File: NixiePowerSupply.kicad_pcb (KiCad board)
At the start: 2 copper layers, 50.8 x 44.4 mm, 20 parts, among them J1 BARREL_JACK, P1 CONN_01X03, P2 CONN_01X02, T1 IRF644, U1 MAX1771

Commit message: Routing complete
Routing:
- net GND: track 38.7 -> 39.5 mm
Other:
- board text added: "+12V SHDN GND"
- board text added: "HV- HV+"
- board text added: "NixMaster 9000 Rev 1.0 Carl Raymond, May 2017"
- board text added: "OUT ADJ. 150-200V"
- board text added: "PWR 12V"
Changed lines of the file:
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@@
-(kicad_pcb (version 4) (host pcbnew 4.0.6)
+(kicad_pcb (version 4) (host pcbnew 4.0.5)
   (general
     (links 32)
-    (no_connects 3)
+    (no_connects 0)
     (area 40.384999 24.805 99.568572 72.195)
     (thickness 1.6)
-    (drawings 4)
+    (drawings 9)
     (tracks 94)
     (zones 0)
@@
   )
   (setup
-    (last_trace_width 1.016)
+    (last_trace_width 0.508)
     (user_trace_width 0.508)
     (user_trace_width 1.016)
@@
     (trace_clearance 0.2)
     (zone_clearance 0.254)
-    (zone_45_only no)
+    (zone_45_only yes)
     (trace_min 0.2)
     (segment_width 0.2)
@@
     (mod_text_size 1 1)
     (mod_text_width 0.15)
-    (pad_size 1.5 1.5)
-    (pad_drill 0.6)
+    (pad_size 3.7 3.7)
+    (pad_drill 3.7)
     (pad_to_mask_clearance 0)
     (aux_axis_origin 0 0)
     (visible_elements 7FFFFFFF)
     (pcbplotparams
-      (layerselection 0x00030_80000001)
-      (usegerberextensions false)
+      (layerselection 0x010f0_80000001)
+      (usegerberextensions true)
       (excludeedgelayer true)
       (linewidth 0.100000)
@@
       (plotinvisibletext false)
       (padsonsilk false)
-      (subtractmaskfromsilk false)
+      (subtractmaskfromsilk true)
       (outputformat 1)
       (mirror false)
-      (drillshape 1)
+      (drillshape 0)
       (scaleselection 1)
       (outputdirectory ""))
@@
     (tags "resistor 0805")
     (attr smd)
-    (fp_text reference R1 (at 3.175 0 360) (layer F.SilkS)
+    (fp_text reference R1 (at -3.302 0 360) (layer F.SilkS)
       (effects (font (size 1 1) (thickness 0.15)))
     )
@@
   (module nixie:Trimpot_Bourns_3214W (layer F.Cu)
     (at 72.771 57.912)
-    (fp_text reference VR1 (at 0.127 3.937) (layer F.SilkS)
+    (fp_text reference VR1 (at 0.10668 -2.9972) (layer F.SilkS)
       (effects (font (size 1 1) (thickness 0.15)))
     )
@@
   (module nixie:L-B82479A1 (layer F.Cu)
     (at 58.928 38.1 45)
-    (fp_text reference L1 (at 7.112 7.112 225) (layer F.SilkS)
+    (fp_text reference L1 (at -6.64539 -6.64539 315) (layer F.SilkS)
       (effects (font (size 1 1) (thickness 0.15)))
     )
@@
     (tags "SOIC 1.27")
     (attr smd)
-    (fp_text reference U1 (at 0 -3.5) (layer F.SilkS)
+    (fp_text reference U1 (at 0 3.937) (layer F.SilkS)
       (effects (font (size 1 1) (thickness 0.15)))
     )
@@
     (tags "capacitor 0805")
     (attr smd)
-    (fp_text reference C2 (at 3.302 -0.127 360) (layer F.SilkS)
+    (fp_text reference C2 (at 4.29768 0.04572 360) (layer F.SilkS)
       (effects (font (size 1 1) (thickness 0.15)))
     )
@@
     (fp_circle (center 0 0) (end 3.7 0) (layer Cmts.User) (width 0.15))
     (fp_circle (center 0 0) (end 3.95 0) (layer F.CrtYd) (width 0.05))
-    (pad 1 np_thru_hole circle (at 0 0) (size 3.7 3.7) (drill 3.7) (layers *.Cu *.Mask))
+    (pad "" np_thru_hole circle (at 0 0) (size 3.7 3.7) (drill 3.7) (layers *.Cu *.Mask))
   )
   (module Resistors_SMD:R_2010_HandSoldering (layer F.Cu)
@@
     (tags "resistor 2010")
     (attr smd)
-    (fp_text reference Rsense1 (at 5.461 -0.254 360) (layer F.SilkS)
+    (fp_text reference Rsense1 (at -1.143 -1.905 450) (layer F.SilkS)
       (effects (font (size 1 1) (thickness 0.15)))
     )
@@
     (descr "SMT capacitor, aluminium electrolytic, 10x10")
     (attr smd)
-    (fp_text reference C4 (at 0 6.46) (layer F.SilkS)
+    (fp_text reference C4 (at -1.524 -6.096) (layer F.SilkS)
       (effects (font (size 1 1) (thickness 0.15)))
     )
@@
     )
   )
+  (gr_text "OUT ADJ.\n150-200V" (at 72.87768 61.63056) (layer F.SilkS)
+    (effects (font (size 0.762 0.762) (thickness 0.1778)))
+  )
+  (gr_text "PWR\n12V" (at 47.625 45.72) (layer F.SilkS)
+    (effects (font (size 1.5 1.5) (thickness 0.3)))
+  )
+  (gr_text "HV-\n\n\n\nHV+" (at 80.01 62.23 90) (layer F.SilkS)
+    (effects (font (size 0.762 1) (thickness 0.1778)))
+  )
+  (gr_text "+12V\n\nSHDN\n\nGND" (at 60.23864 63.70828 90) (layer F.SilkS)
+    (effects (font (size 0.762 1) (thickness 0.1905)) (justify left))
+  )
+  (gr_text "NixMaster 9000 Rev 1.0  \nCarl Raymond, May 2017" (at 55.88 27.94) (layer F.SilkS)
+    (effects (font (size 1.2 1.5) (thickness 0.3)) (justify left))
+  )
   (gr_line (start 95.25 25.4) (end 95.25 69.85) (layer Edge.Cuts) (width 0.1))
   (gr_line (start 44.45 69.85) (end 44.45 25.4) (layer Edge.Cuts) (width 0.1))
   (gr_line (start 95.25 69.85) (end 44.45 69.85) (layer Edge.Cuts) (width 0.1))
   (gr_line (start 44.45 25.4) (end 95.25 25.4) (layer Edge.Cuts) (width 0.1))
+  (segment (start 80.645 52.705) (end 78.74 52.705) (width 0.508) (layer B.Cu) (net 1))
+  (via (at 80.645 50.165) (size 1.016) (drill 0.508) (layers F.Cu B.Cu) (net 1))
+  (segment (start 79.883 49.403) (end 80.645 50.165) (width 0.508) (layer F.Cu) (net 1))
+  (segment (start 79.883 48.108) (end 79.883 49.403) (width 0.508) (layer F.Cu) (net 1))
+  (via (at 78.74 50.165) (size 1.016) (drill 0.508) (layers F.Cu B.Cu) (net 1))
+  (segment (start 80.645 50.165) (end 78.74 50.165) (width 0.508) (layer B.Cu) (net 1))
+  (via (at 78.74 51.435) (size 1.016) (drill 0.508) (layers F.Cu B.Cu) (net 1))
+  (segment (start 78.74 50.165) (end 78.74 51.435) (width 0.508) (layer F.Cu) (net 1))
+  (via (at 80.645 51.435) (size 1.016) (drill 0.508) (layers F.Cu B.Cu) (net 1))
+  (segment (start 78.74 51.435) (end 80.645 51.435) (width 0.508) (layer B.Cu) (net 1))
+  (via (at 80.645 52.705) (size 1.016) (drill 0.508) (layers F.Cu B.Cu) (net 1))
+  (segment (start 80.645 51.435) (end 80.645 52.705) (width 0.508) (layer F.Cu) (net 1))
+  (via (at 78.74 52.705) (size 1.016) (drill 0.508) (layers F.Cu B.Cu) (net 1))
   (segment (start 67.691 59.262) (end 67.691 61.087) (width 1.016) (layer F.Cu) (net 1))
   (via (at 67.691 61.087) (size 0.6) (drill 0.4) (layers F.Cu B.Cu) (net 1))
@@
   (segment (start 67.183 48.748) (end 67.183 50.546) (width 1.016) (layer F.Cu) (net 1))
   (via (at 67.183 50.546) (size 1.016) (drill 0.508) (layers F.Cu B.Cu) (net 1))
-  (via (at 81.28 50.292) (size 1.016) (drill 0.508) (layers F.Cu B.Cu) (net 1))
-  (segment (start 81.28 51.816) (end 81.28 50.292) (width 0.508) (layer B.Cu) (net 1))
-  (segment (start 79.756 51.816) (end 81.28 51.816) (width 0.508) (layer F.Cu) (net 1))
-  (via (at 81.28 51.816) (size 1.016) (drill 0.508) (layers F.Cu B.Cu) (net 1))
-  (segment (start 78.232 51.816) (end 79.756 51.816) (width 0.508) (layer B.Cu) (net 1))
-  (via (at 79.756 51.816) (size 1.016) (drill 0.508) (layers F.Cu B.Cu) (net 1))
-  (segment (start 78.232 50.292) (end 78.232 51.816) (width 0.508) (layer F.Cu) (net 1))
-  (via (at 78.232 51.816) (size 1.016) (drill 0.508) (layers F.Cu B.Cu) (net 1))
-  (segment (start 79.756 50.292) (end 78.232 50.292) (width 0.508) (layer B.Cu) (net 1))
-  (via (at 78.232 50.292) (size 1.016) (drill 0.508) (layers F.Cu B.Cu) (net 1))
-  (segment (start 79.883 48.108) (end 79.883 50.165) (width 0.508) (layer F.Cu) (net 1))
-  (segment (start 79.883 50.165) (end 79.756 50.292) (width 0.508) (layer F.Cu) (net 1))
-  (via (at 79.756 50.292) (size 1.016) (drill 0.508) (layers F.Cu B.Cu) (net 1))
   (segment (start 93.98 44.704) (end 93.98 43.18) (width 0.508) (layer B.Cu) (net 1))
   (via (at 93.98 43.18) (size 1.016) (drill 0.508) (layers F.Cu B.Cu) (net 1))
@@
   (segment (start 53.490349 43.537651) (end 53.490349 48.26) (width 3.81) (layer F.Cu) (net 9))
   (segment (start 53.490349 48.26) (end 53.490349 52.220349) (width 3.81) (layer F.Cu) (net 9))
-  (segment (start 62.738 48.295) (end 53.525349 48.295) (width 2.032) (layer F.Cu) (net 9))
+  (segment (start 62.738 48.295) (end 53.525349 48.295) (width 2.54) (layer F.Cu) (net 9))
   (segment (start 53.525349 48.295) (end 53.490349 48.26) (width 2.032) (layer F.Cu) (net 9))
   (segment (start 57.785 66.04) (end 57.785 56.515) (width 1.524) (layer F.Cu) (net 9))
@@
     (connect_pads (clearance 0.254))
     (min_thickness 0.254)
-    (fill yes (arc_segments 16) (thermal_gap 0.508) (thermal_bridge_width 0.508))
+    (fill yes (arc_segments 16) (thermal_gap 0.508) (thermal_bridge_width 0.508) (smoothing chamfer) (radius 1.27))
     (polygon
       (pts
-        (xy 95.25 25.4) (xy 44.45 25.4) (xy 44.45 69.85) (xy 95.25 69.85)
+        (xy 95.28556 34.91992) (xy 84.95284 35.00628) (xy 85.0392 30.44952) (xy 66.89277 30.48) (xy 66.77152 45.93336)
+        (xy 51.13528 45.99432) (xy 51.13528 35.433) (xy 44.49064 35.47364) (xy 44.45 69.85) (xy 95.25 69.85)
       )
     )
@@
     (connect_pads yes (clearance 0.254))
     (min_thickness 0.254)
-    (fill yes (arc_segments 16) (thermal_gap 0.508) (thermal_bridge_width 0.508) (smoothing chamfer) (radius 0.254))
+    (fill yes (arc_segments 16) (thermal_gap 0.508) (thermal_bridge_width 0.508) (smoothing chamfer) (radius 0.508))
     (polygon
       (pts
@@
     (connect_pads yes (clearance 0.254))
     (min_thickness 0.254)
-    (fill yes (arc_segments 16) (thermal_gap 0.508) (thermal_bridge_width 0.508) (smoothing chamfer) (radius 0.254))
+    (fill yes (arc_segments 16) (thermal_gap 0.508) (thermal_bridge_width 0.508) (smoothing chamfer) (radius 0.508))
     (polygon
       (pts
-        (xy 78.359 45.847) (xy 81.915 45.847) (xy 81.915 52.451) (xy 77.597 52.451) (xy 77.597 47.879)
-        (xy 74.168 47.879) (xy 74.168 45.847)
+        (xy 78.359 45.847) (xy 81.534 45.847) (xy 81.534 53.467) (xy 77.978 53.467) (xy 77.978 47.879)
+        (xy 74.0156 47.86376) (xy 74.0156 45.83176)
       )
     )

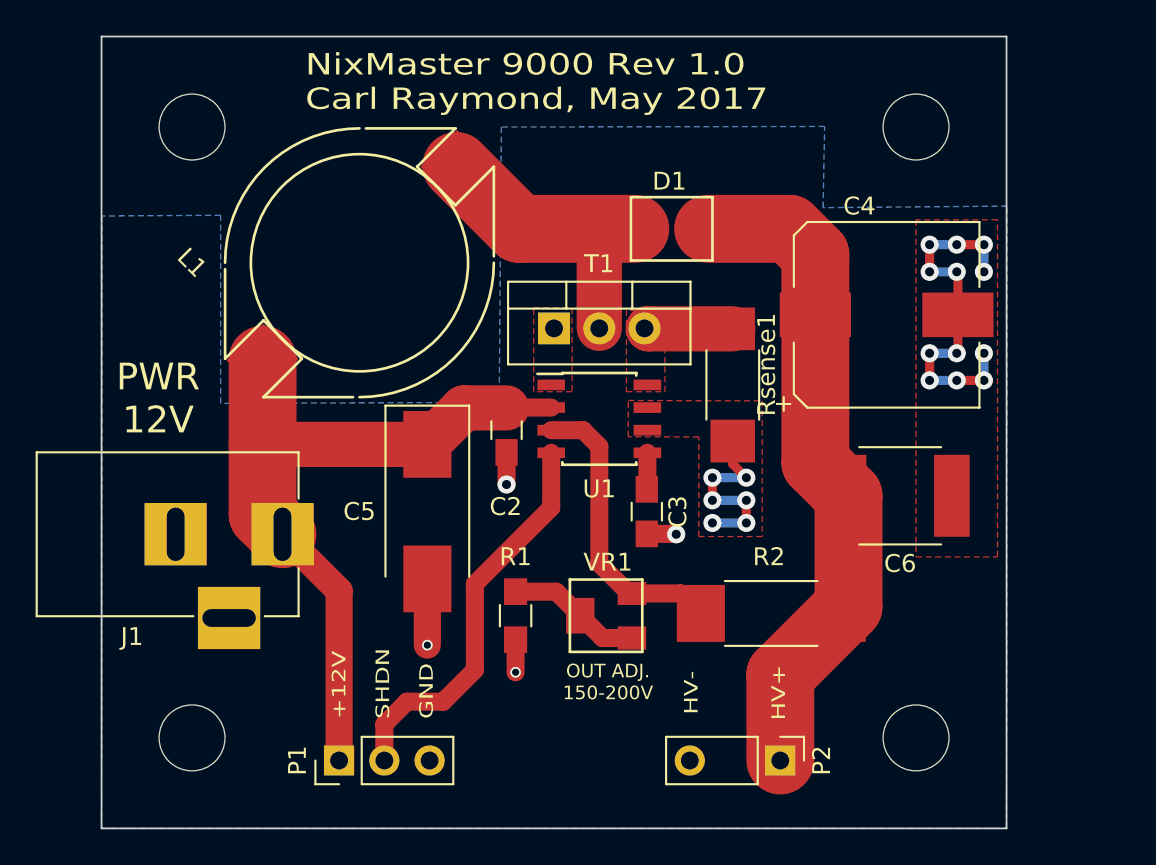
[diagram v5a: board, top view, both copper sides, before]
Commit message: Added missing C1
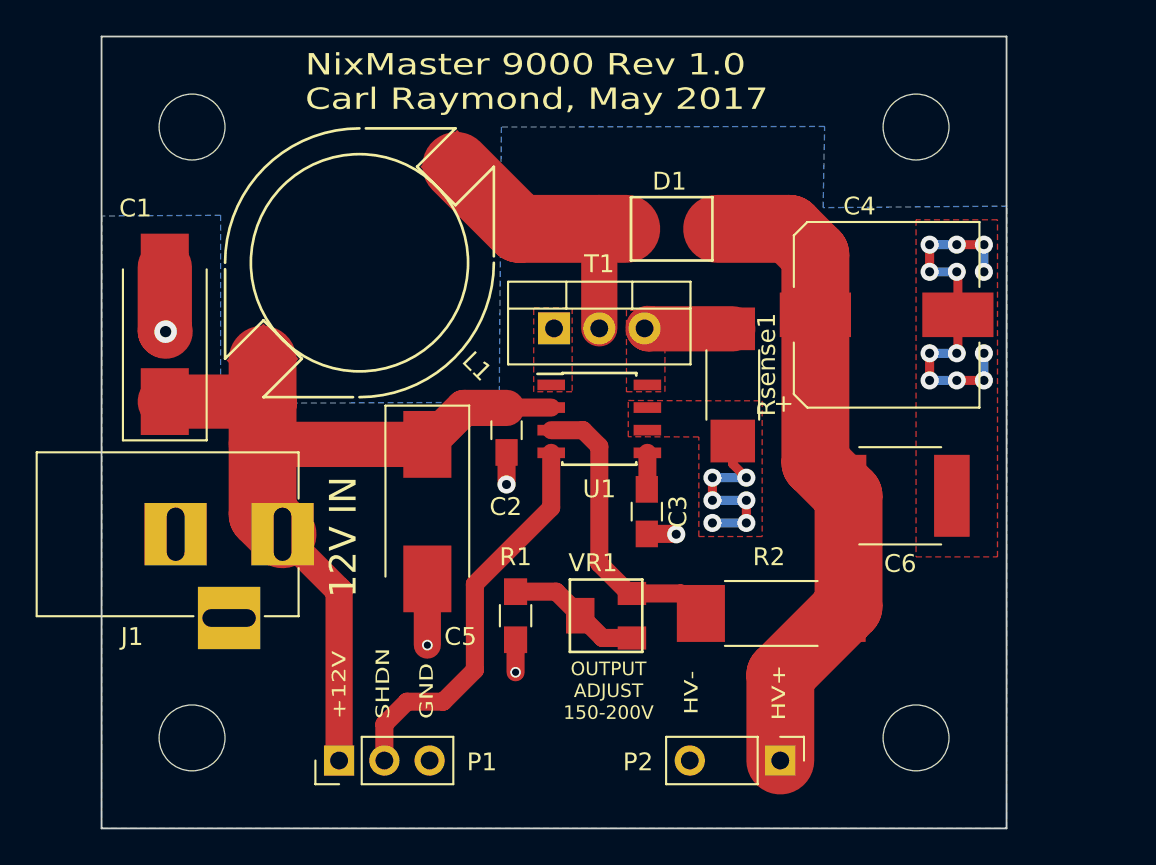
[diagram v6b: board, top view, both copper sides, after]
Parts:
- added C1: 100uF, 35V, Capacitors_Tantalum_SMD:CP_Tantalum_Case-X_EIA-7343-43_Hand, F.Cu at (48.0, 42.1)
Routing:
- net Net-(C1-Pad1): track 41.4 -> 46.9 mm
- net GND: track 39.5 -> 43.1 mm, vias 22 -> 23
- net Net-(D1-Pad2): track 17.1 -> 16.6 mm
- net Net-(C4-Pad1): track 37.4 -> 36.9 mm
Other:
- board text added: "12V IN"
- board text added: "OUTPUT ADJUST 150-200V"
- board text removed: "OUT ADJ. 150-200V"
- board text removed: "PWR 12V"
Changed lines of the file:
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@@
 (kicad_pcb (version 4) (host pcbnew 4.0.5)
   (general
-    (links 32)
+    (links 34)
     (no_connects 0)
     (area 40.384999 24.805 99.568572 72.195)
     (thickness 1.6)
     (drawings 9)
-    (tracks 94)
+    (tracks 100)
     (zones 0)
-    (modules 20)
+    (modules 21)
     (nets 11)
   )
@@
   )
   (setup
-    (last_trace_width 0.508)
+    (last_trace_width 0.25)
     (user_trace_width 0.508)
     (user_trace_width 1.016)
@@
       (drillshape 0)
       (scaleselection 1)
-      (outputdirectory ""))
+      (outputdirectory output/))
   )
   (net 0 "")
@@
     (descr "Through hole straight pin header, 1x03, 2.54mm pitch, single row")
     (tags "Through hole pin header THT 1x03 2.54mm single row")
-    (fp_text reference P2 (at 0 -2.33 270) (layer F.SilkS)
+    (fp_text reference P2 (at 0.08636 7.98576 360) (layer F.SilkS)
       (effects (font (size 1 1) (thickness 0.15)))
     )
@@
   (module nixie:Trimpot_Bourns_3214W (layer F.Cu)
     (at 72.771 57.912)
-    (fp_text reference VR1 (at 0.10668 -2.9972) (layer F.SilkS)
+    (fp_text reference VR1 (at -0.7366 -2.96672) (layer F.SilkS)
       (effects (font (size 1 1) (thickness 0.15)))
     )
@@
       (net 5 "Net-(R1-Pad1)"))
     (model "/Users/carl/Documents/KiCad/NixiePowerSupply/models/Bourns 3214W.wrl"
-      (at (xyz 0 0 0))
-      (scale (xyz 1 1 1))
-      (rotate (xyz 0 0 0))
+      (at (xyz 0.065 -0.01 0.11))
+      (scale (xyz 0.3937 0.3937 0.3937))
+      (rotate (xyz 90 0 90))
     )
   )
@@
   (module nixie:L-B82479A1 (layer F.Cu)
     (at 58.928 38.1 45)
-    (fp_text reference L1 (at -6.64539 -6.64539 315) (layer F.SilkS)
+    (fp_text reference L1 (at 0.556776 8.775506 315) (layer F.SilkS)
       (effects (font (size 1 1) (thickness 0.15)))
     )
@@
     (tags "capacitor tantalum smd")
     (attr smd)
-    (fp_text reference C5 (at 0 3.81 360) (layer F.SilkS)
+    (fp_text reference C5 (at 7.01548 -1.85928 360) (layer F.SilkS)
       (effects (font (size 1 1) (thickness 0.15)))
     )
@@
     (descr "Through hole straight pin header, 1x03, 2.54mm pitch, single row")
     (tags "Through hole pin header THT 1x03 2.54mm single row")
-    (fp_text reference P1 (at 0 -2.33 90) (layer F.SilkS)
+    (fp_text reference P1 (at -0.08636 8.01624 180) (layer F.SilkS)
       (effects (font (size 1 1) (thickness 0.15)))
     )
@@
     )
   )
-  (gr_text "OUT ADJ.\n150-200V" (at 72.87768 61.63056) (layer F.SilkS)
-    (effects (font (size 0.762 0.762) (thickness 0.1778)))
-  )
-  (gr_text "PWR\n12V" (at 47.625 45.72) (layer F.SilkS)
+  (module Capacitors_Tantalum_SMD:CP_Tantalum_Case-X_EIA-7343-43_Hand (layer F.Cu)
+    (at 48.00092 42.11828 90)
+    (descr "Tantalum capacitor, Case X, EIA 7343-43, 7.3x4.2x4.0mm, Hand soldering footprint")
+    (tags "capacitor tantalum smd")
+    (attr smd)
+    (fp_text reference C1 (at 7.08152 -1.651 180) (layer F.SilkS)
+      (effects (font (size 1 1) (thickness 0.15)))
+    )
+    (fp_text value "100uF, 35V" (at 0 3.85 90) (layer F.Fab)
+      (effects (font (size 1 1) (thickness 0.15)))
+    )
+    (fp_line (start -6.05 -2.5) (end -6.05 2.5) (layer F.CrtYd) (width 0.05))
+    (fp_line (start -6.05 2.5) (end 6.05 2.5) (layer F.CrtYd) (width 0.05))
+    (fp_line (start 6.05 2.5) (end 6.05 -2.5) (layer F.CrtYd) (width 0.05))
+    (fp_line (start 6.05 -2.5) (end -6.05 -2.5) (layer F.CrtYd) (width 0.05))
+    (fp_line (start -3.65 -2.1) (end -3.65 2.1) (layer F.Fab) (width 0.1))
+    (fp_line (start -3.65 2.1) (end 3.65 2.1) (layer F.Fab) (width 0.1))
+    (fp_line (start 3.65 2.1) (end 3.65 -2.1) (layer F.Fab) (width 0.1))
+    (fp_line (start 3.65 -2.1) (end -3.65 -2.1) (layer F.Fab) (width 0.1))
+    (fp_line (start -2.92 -2.1) (end -2.92 2.1) (layer F.Fab) (width 0.1))
+    (fp_line (start -2.555 -2.1) (end -2.555 2.1) (layer F.Fab) (width 0.1))
+    (fp_line (start -5.95 -2.35) (end 3.65 -2.35) (layer F.SilkS) (width 0.12))
+    (fp_line (start -5.95 2.35) (end 3.65 2.35) (layer F.SilkS) (width 0.12))
+    (fp_line (start -5.95 -2.35) (end -5.95 2.35) (layer F.SilkS) (width 0.12))
+    (pad 1 smd rect (at -3.775 0 90) (size 3.75 2.7) (layers F.Cu F.Paste F.Mask)
+      (net 9 "Net-(C1-Pad1)"))
+    (pad 2 smd rect (at 3.775 0 90) (size 3.75 2.7) (layers F.Cu F.Paste F.Mask)
+      (net 1 GND))
+    (model Capacitors_Tantalum_SMD.3dshapes/CP_Tantalum_Case-X_EIA-7343-43.wrl
+      (at (xyz 0 0 0))
+      (scale (xyz 1 1 1))
+      (rotate (xyz 0 0 0))
+    )
+  )
+  (gr_text "OUTPUT\nADJUST\n150-200V" (at 72.90816 62.12332) (layer F.SilkS)
+    (effects (font (size 0.762 0.762) (thickness 0.1905)))
+  )
+  (gr_text "12V IN" (at 58.01868 53.49748 90) (layer F.SilkS)
     (effects (font (size 1.5 1.5) (thickness 0.3)))
   )
@@
   (gr_line (start 95.25 69.85) (end 44.45 69.85) (layer Edge.Cuts) (width 0.1))
   (gr_line (start 44.45 25.4) (end 95.25 25.4) (layer Edge.Cuts) (width 0.1))
+  (segment (start 48.00092 38.34328) (end 48.00092 41.92016) (width 3.048) (layer F.Cu) (net 1))
+  (segment (start 48.00092 41.92016) (end 48.04664 41.96588) (width 3.048) (layer F.Cu) (net 1))
+  (via (at 48.04664 41.96588) (size 1.27) (drill 0.635) (layers F.Cu B.Cu) (net 1))
   (segment (start 80.645 52.705) (end 78.74 52.705) (width 0.508) (layer B.Cu) (net 1))
   (via (at 80.645 50.165) (size 1.016) (drill 0.508) (layers F.Cu B.Cu) (net 1))
@@
   (segment (start 84.519 41.021) (end 84.519 49.319) (width 3.81) (layer F.Cu) (net 3))
   (segment (start 84.519 49.319) (end 86.381 51.181) (width 3.81) (layer F.Cu) (net 3))
-  (segment (start 78.494 36.195) (end 83.066 36.195) (width 3.81) (layer F.Cu) (net 3))
+  (segment (start 79.002 36.195) (end 83.066 36.195) (width 3.81) (layer F.Cu) (net 3))
   (segment (start 83.066 36.195) (end 84.519 37.648) (width 3.81) (layer F.Cu) (net 3))
   (segment (start 84.519 37.648) (end 84.519 41.021) (width 3.81) (layer F.Cu) (net 3))
-  (segment (start 74.414 36.195) (end 72.39 36.195) (width 3.81) (layer F.Cu) (net 4))
+  (segment (start 73.906 36.195) (end 72.39 36.195) (width 3.81) (layer F.Cu) (net 4))
   (segment (start 72.39 36.195) (end 67.898302 36.195) (width 3.81) (layer F.Cu) (net 4))
-  (segment (start 72.39 41.783) (end 72.39 36.195) (width 2.54) (layer F.Cu) (net 4))
+  (segment (start 72.39 41.783) (end 72.39 36.195) (width 2.032) (layer F.Cu) (net 4))
   (segment (start 67.898302 36.195) (end 64.365651 32.662349) (width 3.81) (layer F.Cu) (net 4))
   (segment (start 67.691 56.562) (end 69.971 56.562) (width 1.016) (layer F.Cu) (net 5))
@@
   (segment (start 79.883 41.808) (end 75.15501 41.808) (width 2.54) (layer F.Cu) (net 7))
   (segment (start 75.15501 41.808) (end 75.13001 41.783) (width 2.54) (layer F.Cu) (net 7))
-  (segment (start 62.738 48.295) (end 64.785 46.248) (width 2.54) (layer F.Cu) (net 9))
-  (segment (start 64.785 46.248) (end 67.183 46.248) (width 2.54) (layer F.Cu) (net 9))
+  (segment (start 53.490349 43.537651) (end 53.490349 45.9994) (width 3.81) (layer F.Cu) (net 9))
+  (segment (start 53.490349 45.9994) (end 53.490349 48.26) (width 3.81) (layer F.Cu) (net 9))
+  (segment (start 48.00092 45.89328) (end 53.384229 45.89328) (width 3.048) (layer F.Cu) (net 9))
+  (segment (start 53.384229 45.89328) (end 53.490349 45.9994) (width 3.81) (layer F.Cu) (net 9))
+  (segment (start 62.738 48.295) (end 64.785 46.248) (width 2.032) (layer F.Cu) (net 9))
+  (segment (start 64.785 46.248) (end 67.183 46.248) (width 2.032) (layer F.Cu) (net 9))
   (segment (start 69.69 46.228) (end 67.203 46.228) (width 1.016) (layer F.Cu) (net 9))
   (segment (start 67.203 46.228) (end 67.183 46.248) (width 1.016) (layer F.Cu) (net 9))
-  (segment (start 53.490349 43.537651) (end 53.490349 48.26) (width 3.81) (layer F.Cu) (net 9))
   (segment (start 53.490349 48.26) (end 53.490349 52.220349) (width 3.81) (layer F.Cu) (net 9))
   (segment (start 62.738 48.295) (end 53.525349 48.295) (width 2.54) (layer F.Cu) (net 9))
